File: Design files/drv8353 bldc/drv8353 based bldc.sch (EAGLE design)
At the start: 127 parts, among them IC1 DRV8353RSRGZT, J4 B06B-HCMKK

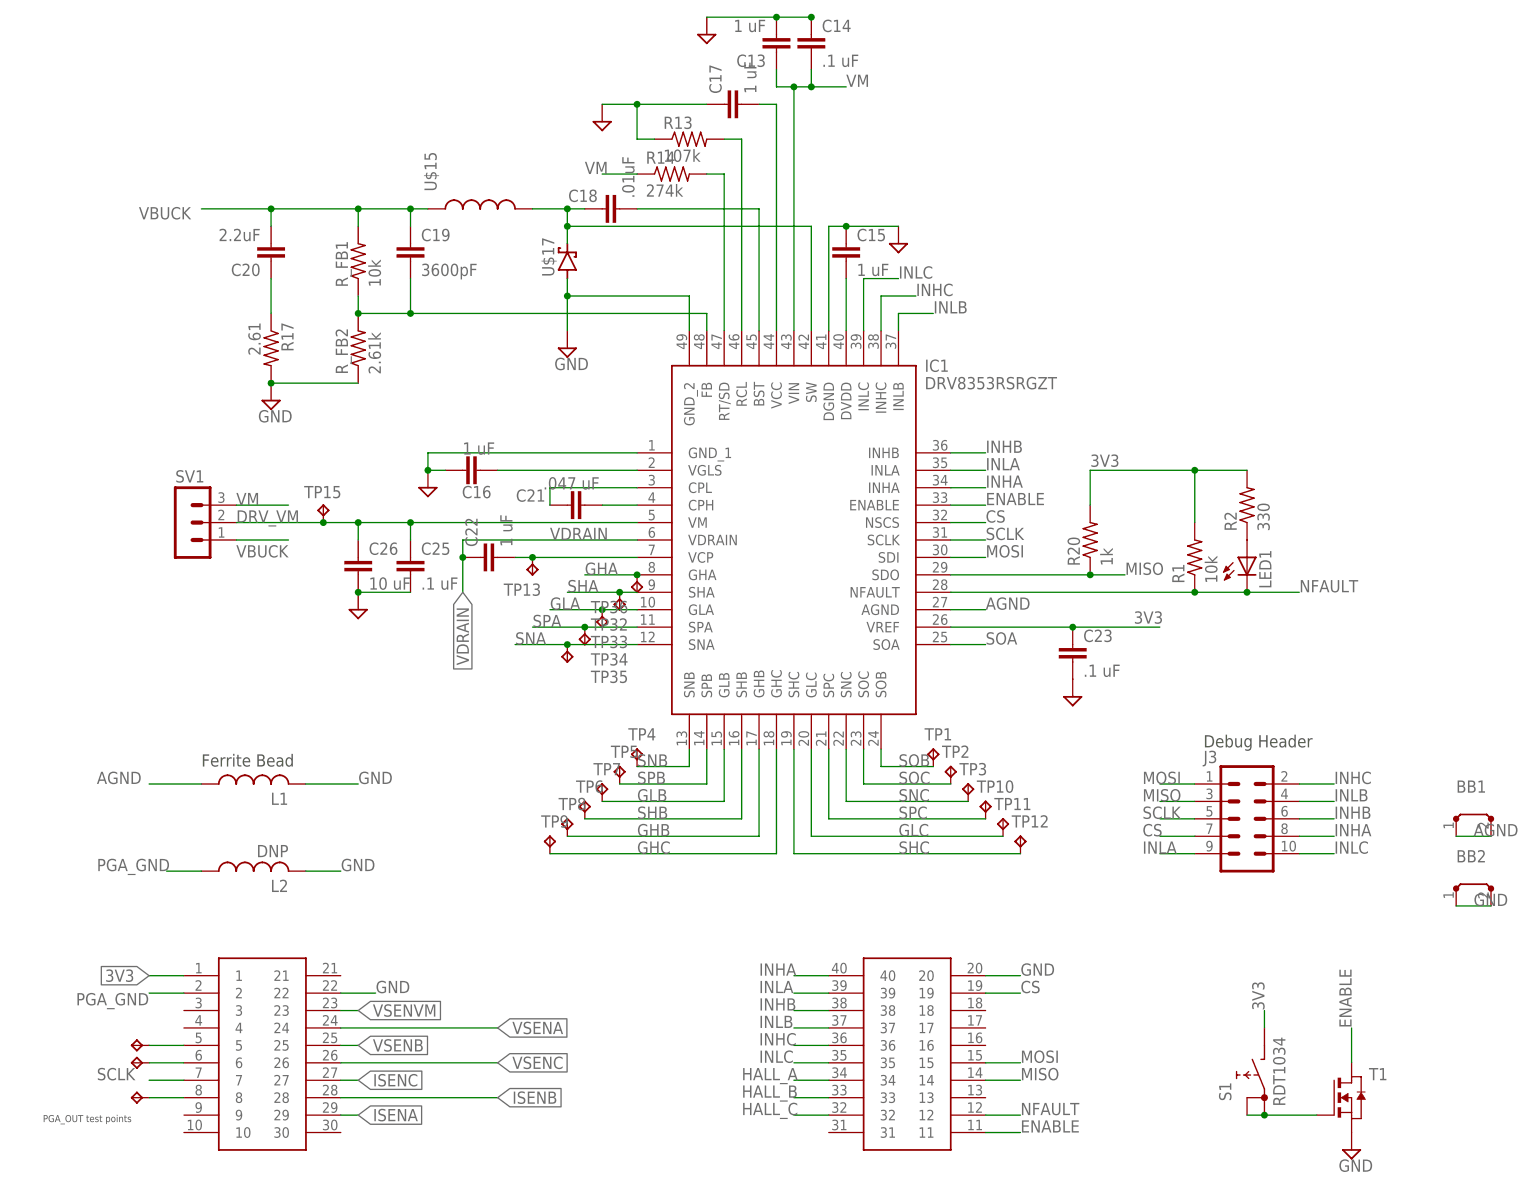
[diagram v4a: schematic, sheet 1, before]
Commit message: modifies power button, debug header, AGND
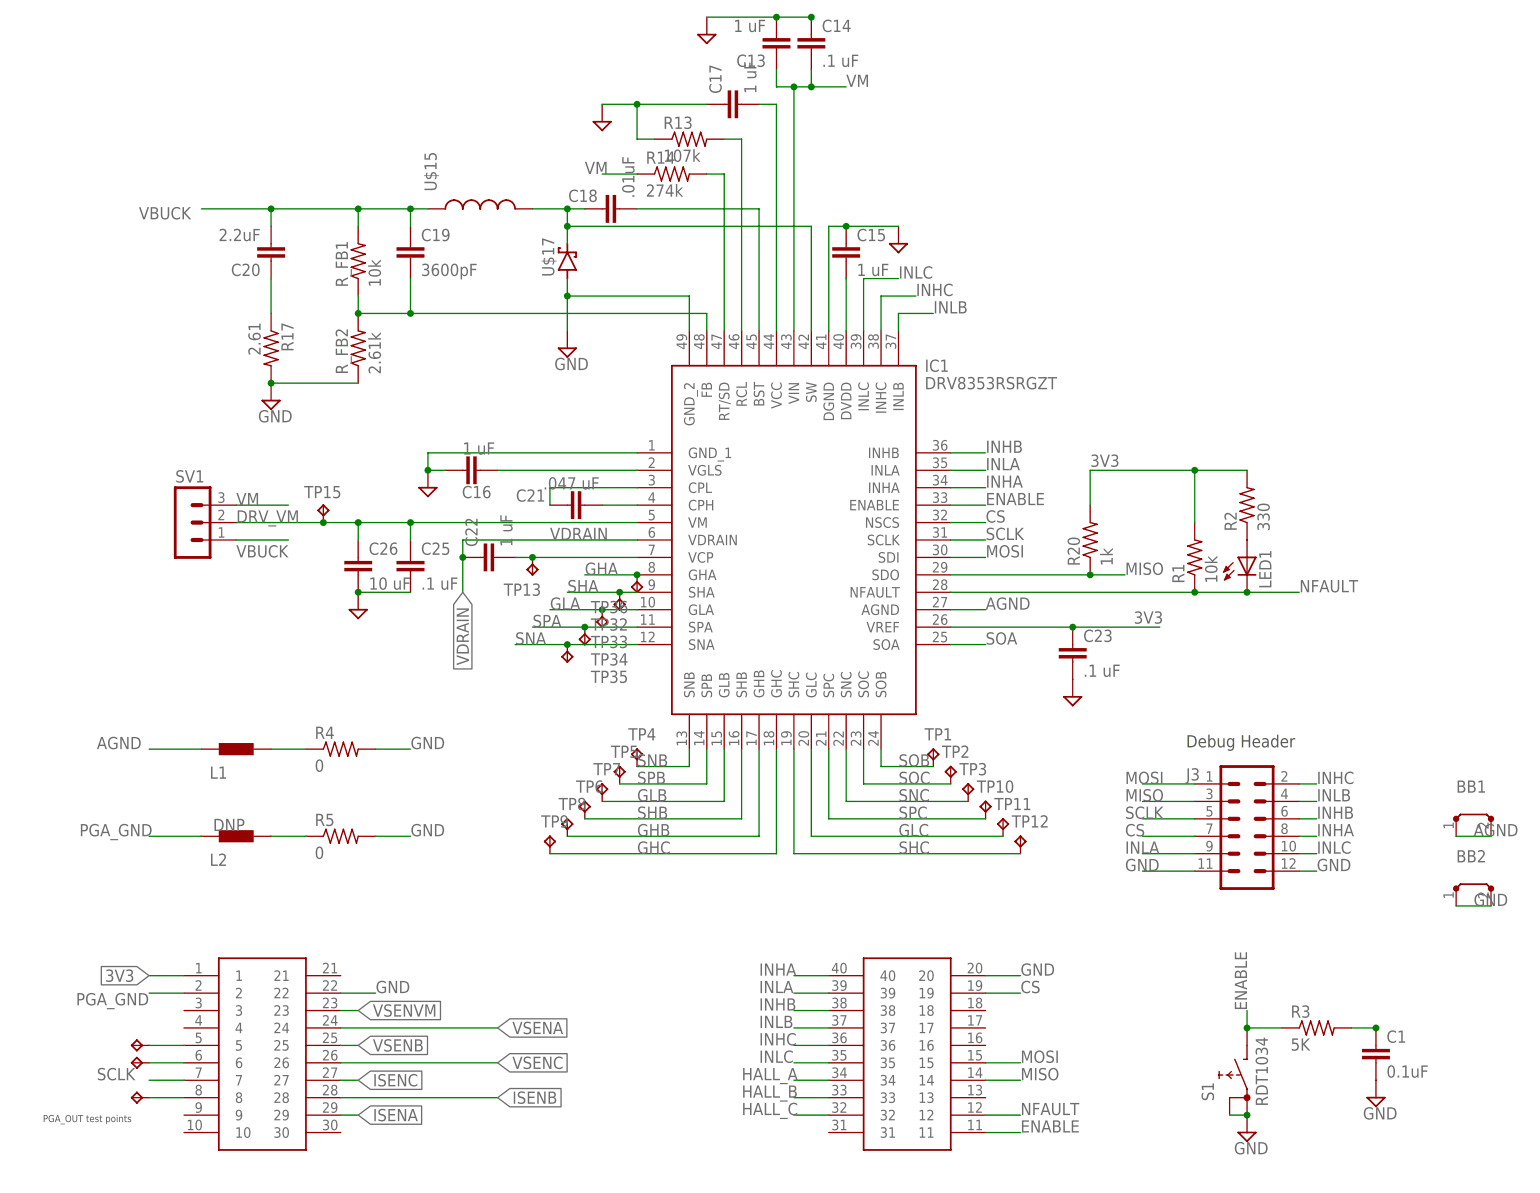
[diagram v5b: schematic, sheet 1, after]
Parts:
- removed T1: (no value), zetex:NMOSSOT23
- added C1: 0.1uF, resistor:C-EUC0603K
- added R3: 5K, resistor:R-US_R0603
- added R4, R5: 0, resistor:R-US_R0603
- J3: value (none) -> 2X6 FEMALE; device SparkFun-Connectors:CONN_05X2NO_SILK -> SparkFun-Connectors:CONN_06X2PTH_FEMALE
- L1: value (none) -> BLM15HB121SN1; device rcl:L-US0204/7 -> inductors:BLM15HB121SN1
- L2: device rcl:L-US0204/7 -> inductors:BLM15HB121SN1
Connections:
- new net N$21: L1.2, R4.1
- new net N$23: L2.2, R5.1
- net 3V3: no longer S1.B
- net ENABLE: now also R3.1, S1.B; no longer T1.D
- net GND: now also C1.2, J3.11, J3.12, R4.2, R5.2, S1.A, S1.A1; no longer L1.2, L2.2, T1.S
- net N$20: now also C1.1, R3.2; no longer S1.A, S1.A1, T1.G
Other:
- note removed: "Ferrite Bead"
- moved on the sheet: S1

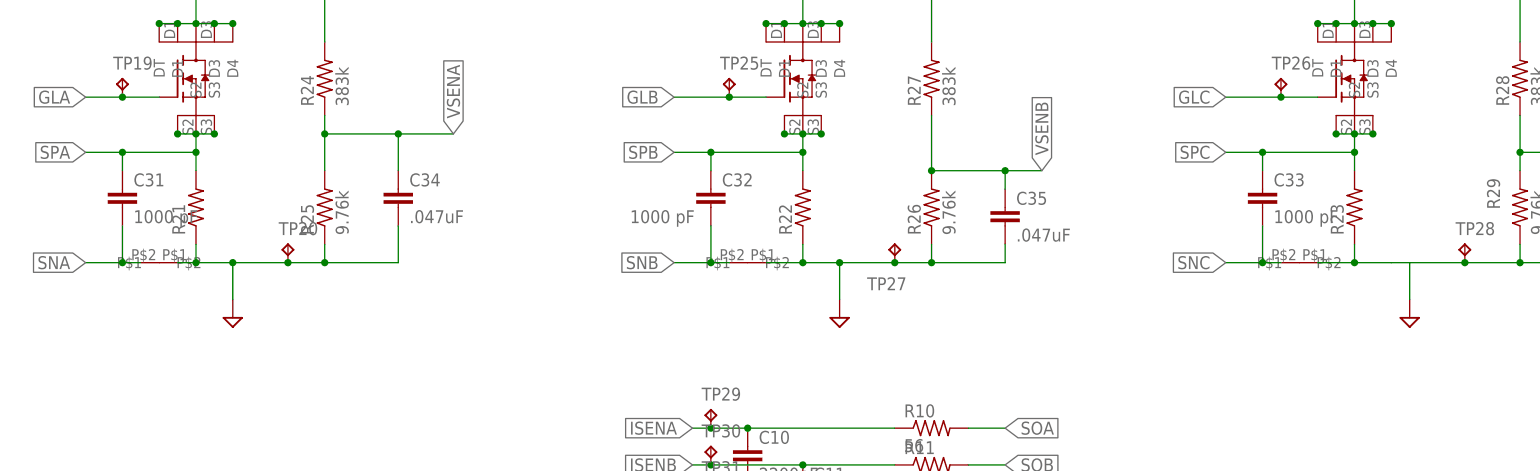
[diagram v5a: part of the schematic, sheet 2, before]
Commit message: added tenative current sense resistor and modified schematic to use kelvin stly current shunt
current shunt is still valueless, but the package suports the range of 2-3 mohm with a tolerence of either .1% or .5%. a very similar package can do 1-2 mohm if we decide that's what we want.
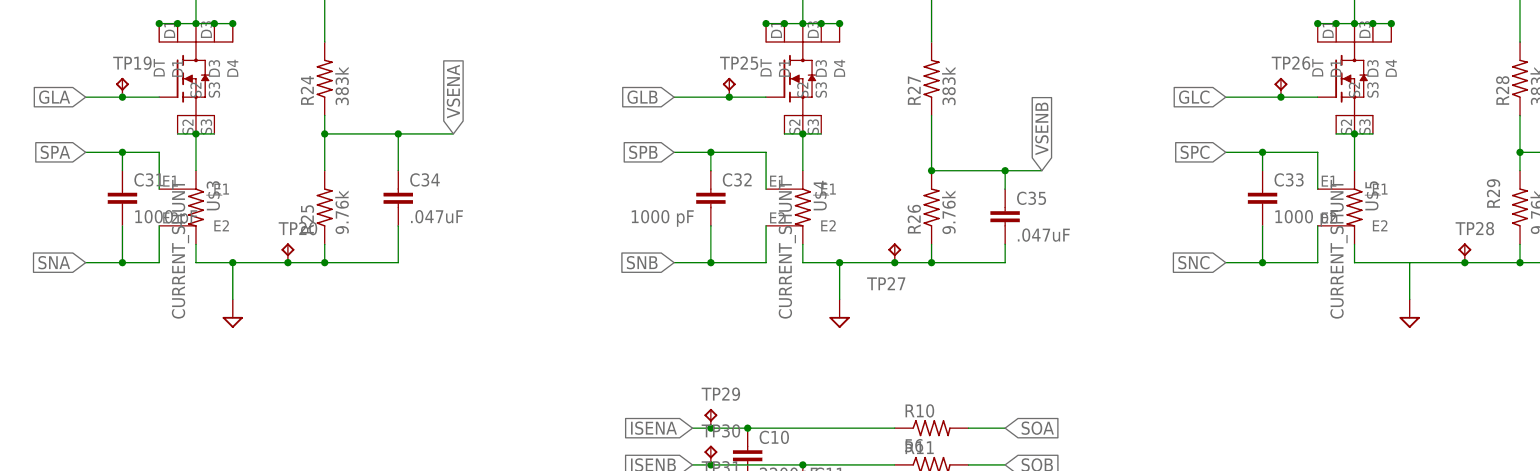
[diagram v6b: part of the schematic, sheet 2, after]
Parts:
- removed R21, R22, R23: (no value), rcl:R-US_R2512
- removed U$26, U$28, U$29: NET_TIE, REV BLDC:NET_TIE
- added U$3, U$4, U$5: CURRENT_SHUNT, REV BLDC:CURRENT_SHUNT
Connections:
- new net N$22: U$21.S1, U$21.S2, U$21.S3, U$4.I1
- new net N$24: U$20.S1, U$20.S2, U$20.S3, U$3.I1
- new net N$27: U$24.S1, U$24.S2, U$24.S3, U$5.I1
- net GND: now also U$3.I2, U$4.I2, U$5.I2; no longer R21.1, R22.1, R23.1, U$26.P$1, U$28.P$1, U$29.P$1
- net SNA: now also U$3.E2; no longer U$26.P$2
- net SNB: now also U$4.E2; no longer U$28.P$2
- net SNC: now also U$5.E2; no longer U$29.P$2
- net SPA: now also U$3.E1; no longer R21.2, U$20.S1, U$20.S2, U$20.S3
- net SPB: now also U$4.E1; no longer R22.2, U$21.S1, U$21.S2, U$21.S3
- net SPC: now also U$5.E1; no longer R23.2, U$24.S1, U$24.S2, U$24.S3

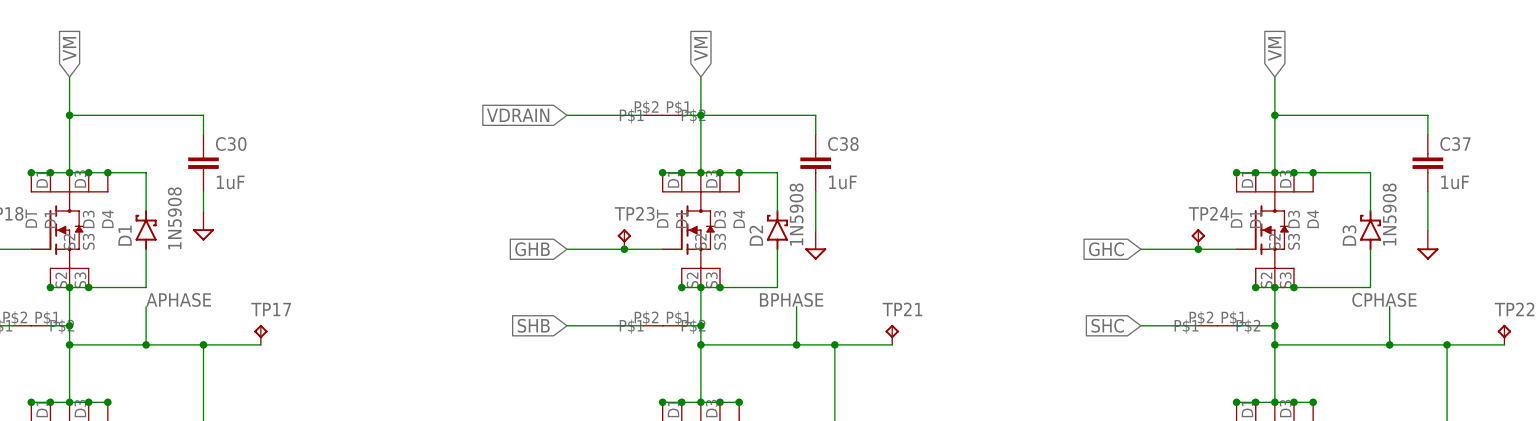
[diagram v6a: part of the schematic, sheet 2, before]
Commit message: changes board grid to 1 mm, 0.1mm grid, changes package for schottky diodes
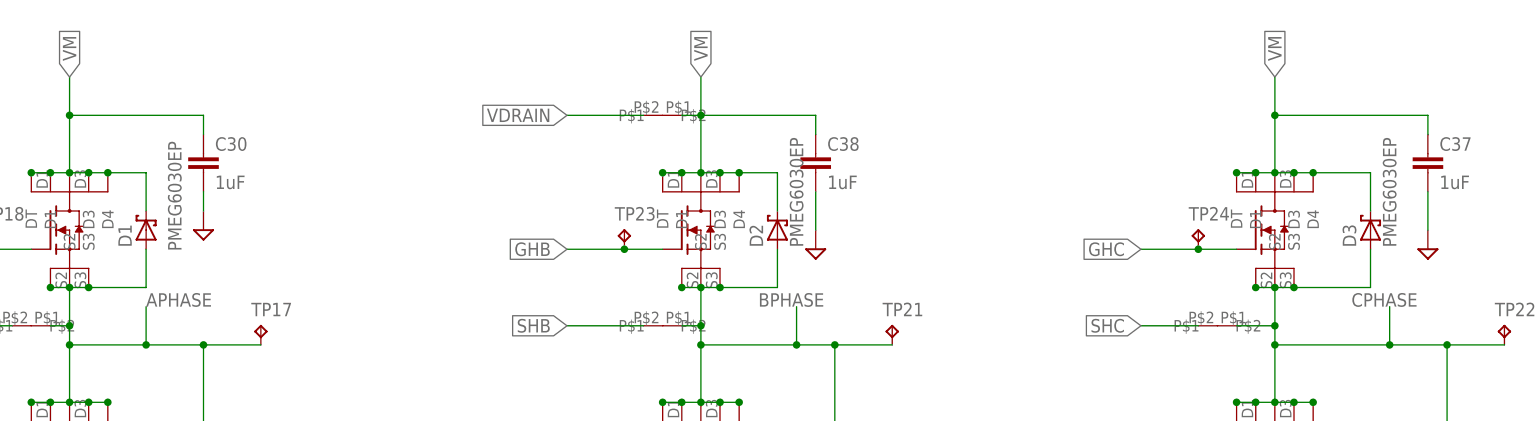
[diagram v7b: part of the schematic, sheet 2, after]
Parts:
- D1, D2, D3: value 1N5908 -> PMEG6030EP; device diode:1N5908 -> nxp_60:PMEG6030EP
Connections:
- net VM: now also D1.K, D2.K, D3.K; no longer D1.C, D2.C, D3.C

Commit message: finalizes package of schottky diodes
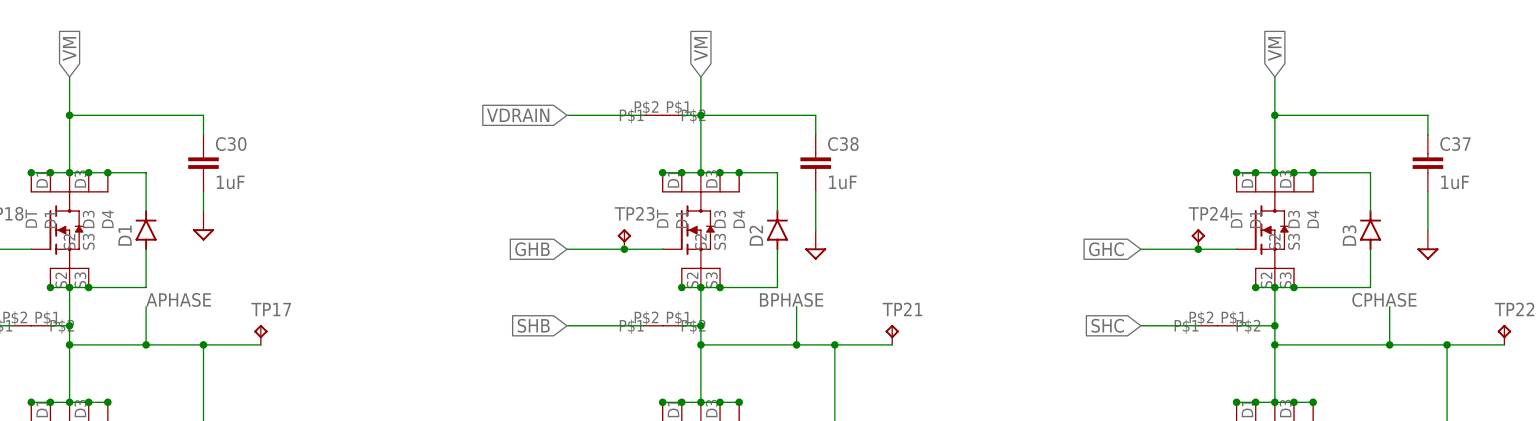
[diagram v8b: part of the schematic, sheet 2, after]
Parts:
- D1, D2, D3: value PMEG6030EP -> (none); device nxp_60:PMEG6030EP -> semicon-smd-ipc:D-SOD123
- L1: value BLM15HB121SN1 -> 33nH/±5%/500mA; device inductors:BLM15HB121SN1 -> SparkFun-Coils:INDUCTOR-0603-33NH
- L2: device inductors:BLM15HB121SN1 -> SparkFun-Coils:INDUCTOR-0603-33NH
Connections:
- net VM: now also D1.C, D2.C, D3.C; no longer D1.K, D2.K, D3.K
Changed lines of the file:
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@@
 <part name="R1" library="rcl" library_urn="urn:adsk.eagle:library:334" deviceset="R-US_" device="R0603" package3d_urn="urn:adsk.eagle:package:23555/3" value="10k"/>
 <part name="R2" library="rcl" library_urn="urn:adsk.eagle:library:334" deviceset="R-US_" device="R0603" package3d_urn="urn:adsk.eagle:package:23555/3" value="330"/>
-<part name="D1" library="nxp_60" deviceset="PMEG6030" device="EP"/>
-<part name="D2" library="nxp_60" deviceset="PMEG6030" device="EP"/>
-<part name="D3" library="nxp_60" deviceset="PMEG6030" device="EP"/>
+<part name="D1" library="semicon-smd-ipc" library_urn="urn:adsk.eagle:library:353" deviceset="D-" device="SOD123" package3d_urn="urn:adsk.eagle:package:26308/2"/>
+<part name="D2" library="semicon-smd-ipc" library_urn="urn:adsk.eagle:library:353" deviceset="D-" device="SOD123" package3d_urn="urn:adsk.eagle:package:26308/2"/>
+<part name="D3" library="semicon-smd-ipc" library_urn="urn:adsk.eagle:library:353" deviceset="D-" device="SOD123" package3d_urn="urn:adsk.eagle:package:26308/2"/>
 <part name="SUPPLY8" library="supply2" library_urn="urn:adsk.eagle:library:372" deviceset="GND" device=""/>
 <part name="TP1" library="testpad" library_urn="urn:adsk.eagle:library:385" deviceset="TP" device="B1,27" package3d_urn="urn:adsk.eagle:package:27944/2"/>
@@
 <part name="SUPPLY11" library="supply2" library_urn="urn:adsk.eagle:library:372" deviceset="GND" device=""/>
 <part name="R3" library="resistor" library_urn="urn:adsk.eagle:library:348" deviceset="R-US_" device="R0603" package3d_urn="urn:adsk.eagle:package:26057/1" value="5K"/>
-<part name="L2" library="inductors" library_urn="urn:adsk.eagle:library:243" deviceset="BLM15H" device="" package3d_urn="urn:adsk.eagle:package:15132/1" technology="B121SN1" value="DNP"/>
-<part name="L1" library="inductors" library_urn="urn:adsk.eagle:library:243" deviceset="BLM15H" device="" package3d_urn="urn:adsk.eagle:package:15132/1" technology="B121SN1"/>
+<part name="L2" library="SparkFun-Coils" library_urn="urn:adsk.eagle:library:512" deviceset="INDUCTOR" device="-0603-33NH" package3d_urn="urn:adsk.eagle:package:37574/1" value="DNP"/>
+<part name="L1" library="SparkFun-Coils" library_urn="urn:adsk.eagle:library:512" deviceset="INDUCTOR" device="-0603-33NH" package3d_urn="urn:adsk.eagle:package:37574/1" value="33nH/±5%/500mA"/>
 <part name="R4" library="resistor" library_urn="urn:adsk.eagle:library:348" deviceset="R-US_" device="R0603" package3d_urn="urn:adsk.eagle:package:26057/1" value="0"/>
 <part name="R5" library="resistor" library_urn="urn:adsk.eagle:library:348" deviceset="R-US_" device="R0603" package3d_urn="urn:adsk.eagle:package:26057/1" value="0"/>
@@
 <attribute name="VALUE" x="92.71" y="-127.762" size="1.778" layer="96"/>
 </instance>
-<instance part="L2" gate="G$1" x="-60.96" y="-96.52" smashed="yes">
-<attribute name="NAME" x="-62.23" y="-99.06" size="1.778" layer="95" rot="R180"/>
-<attribute name="VALUE" x="-59.69" y="-93.98" size="1.778" layer="96" rot="R180"/>
-</instance>
-<instance part="L1" gate="G$1" x="-60.96" y="-83.82" smashed="yes">
-<attribute name="NAME" x="-62.23" y="-86.36" size="1.778" layer="95" rot="R180"/>
+<instance part="L2" gate="G$1" x="-60.96" y="-96.52" smashed="yes" rot="R90">
+<attribute name="NAME" x="-58.42" y="-97.79" size="1.778" layer="95" rot="R270"/>
+<attribute name="VALUE" x="-63.5" y="-95.25" size="1.778" layer="96" rot="R270"/>
+</instance>
+<instance part="L1" gate="G$1" x="-60.96" y="-83.82" smashed="yes" rot="R90">
+<attribute name="NAME" x="-58.42" y="-85.09" size="1.778" layer="95" rot="R270"/>
 </instance>
 <instance part="R4" gate="G$1" x="-45.72" y="-83.82" smashed="yes">
@@
 <wire x1="-55.88" y1="76.2" x2="-55.88" y2="81.28" width="0.1524" layer="91"/>
 <label x="-55.88" y="81.28" size="1.778" layer="95" rot="R90" xref="yes"/>
-<pinref part="D1" gate="G$1" pin="K"/>
+<pinref part="D1" gate="G$1" pin="C"/>
 <wire x1="-45.72" y1="63.5" x2="-45.72" y2="68.58" width="0.1524" layer="91"/>
 <wire x1="-45.72" y1="68.58" x2="-50.8" y2="68.58" width="0.1524" layer="91"/>
@@
 <wire x1="27.94" y1="76.2" x2="27.94" y2="81.28" width="0.1524" layer="91"/>
 <label x="27.94" y="81.28" size="1.778" layer="95" rot="R90" xref="yes"/>
-<pinref part="D2" gate="G$1" pin="K"/>
+<pinref part="D2" gate="G$1" pin="C"/>
 <wire x1="38.1" y1="63.5" x2="38.1" y2="68.58" width="0.1524" layer="91"/>
 <wire x1="38.1" y1="68.58" x2="33.02" y2="68.58" width="0.1524" layer="91"/>
@@
 <junction x="104.14" y="76.2"/>
 <label x="104.14" y="81.28" size="1.778" layer="95" rot="R90" xref="yes"/>
-<pinref part="D3" gate="G$1" pin="K"/>
+<pinref part="D3" gate="G$1" pin="C"/>
 <wire x1="116.84" y1="63.5" x2="116.84" y2="68.58" width="0.1524" layer="91"/>
 <wire x1="116.84" y1="68.58" x2="109.22" y2="68.58" width="0.1524" layer="91"/>
